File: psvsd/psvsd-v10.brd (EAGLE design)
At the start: 30 x 33.4 mm, 30 parts, among them J1 TRANSFLASH-PUSH, U1 USB2244QFN, U3 VREG, Y1 24.000MHz

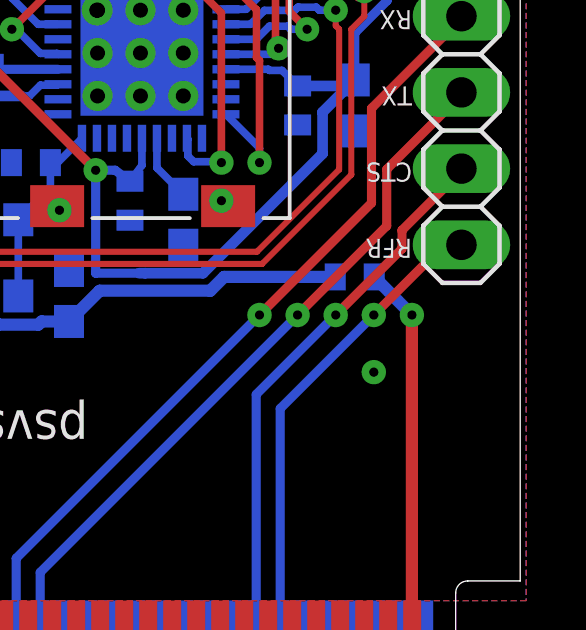
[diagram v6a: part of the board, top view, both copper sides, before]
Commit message: Extended ground plane on top layer to even electric properties
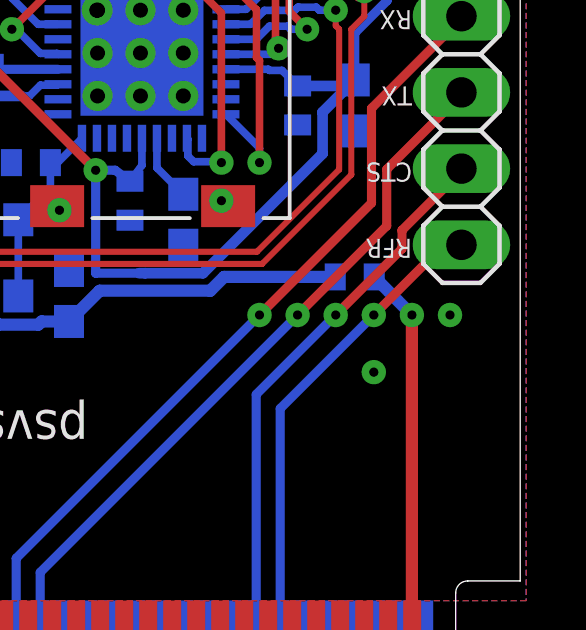
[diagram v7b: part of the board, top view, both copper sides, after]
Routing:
- net GND: vias 20 -> 21
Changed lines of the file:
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@@
 <via x="16.1925" y="17.4625" extent="1-16" drill="0.3048"/>
 <contactref element="R6" pad="2"/>
+<via x="29.21" y="13.97" extent="1-16" drill="0.3048"/>
+<wire x1="23.414" y1="30.75" x2="28.65" y2="32.405" width="0" layer="19" extent="1-1"/>
+<wire x1="23.1775" y1="31.33" x2="23.414" y2="30.75" width="0" layer="19" extent="1-16"/>
+<wire x1="20.97" y1="31.75" x2="23.1775" y2="31.33" width="0" layer="19" extent="16-16"/>
+<wire x1="20.32" y1="30.06" x2="20.97" y2="31.75" width="0" layer="19" extent="16-16"/>
+<wire x1="21.59" y1="29.2608" x2="20.32" y2="30.06" width="0" layer="19" extent="16-16"/>
+<wire x1="20.424" y1="28.1" x2="21.59" y2="29.2608" width="0" layer="19" extent="1-1"/>
+<wire x1="23.71" y1="27.94" x2="21.59" y2="29.2608" width="0" layer="19" extent="16-16"/>
+<wire x1="26.685" y1="26.67" x2="23.71" y2="27.94" width="0" layer="19" extent="16-16"/>
+<wire x1="29.591" y1="26.47" x2="26.685" y2="26.67" width="0" layer="19" extent="16-16"/>
+<wire x1="17.942" y1="25.46" x2="20.424" y2="28.1" width="0" layer="19" extent="1-16"/>
 <wire x1="18.89125" y1="24.13" x2="18.415" y2="24.430025" width="0" layer="19" extent="16-16"/>
-<wire x1="21.59" y1="17.78" x2="21.814" y2="17.6" width="0" layer="19" extent="1-1"/>
-<wire x1="16.35" y1="3.255" x2="15.95" y2="3.255" width="0" layer="19" extent="1-16"/>
-<wire x1="23.1775" y1="31.33" x2="23.414" y2="30.75" width="0" layer="19" extent="1-16"/>
-<wire x1="17.1125125" y1="24.7325125" x2="17.4371" y2="24.13" width="0" layer="19" extent="16-16"/>
+<wire x1="17.1125125" y1="24.7325125" x2="17.9718" y2="24.873225" width="0" layer="19" extent="16-16"/>
+<wire x1="17.4371" y1="24.13" x2="17.1125125" y2="24.7325125" width="0" layer="19" extent="16-16"/>
+<wire x1="17.4625" y1="24.13" x2="17.4371" y2="24.13" width="0" layer="19" extent="1-1"/>
+<wire x1="18.89125" y1="22.70125" x2="18.415" y2="23.495" width="0" layer="19" extent="16-16"/>
+<wire x1="18.942" y1="22.66" x2="18.89125" y2="22.70125" width="0" layer="19" extent="16-16"/>
+<wire x1="17.4625" y1="22.70125" x2="18.415" y2="23.495" width="0" layer="19" extent="16-16"/>
+<wire x1="20.32" y1="22.70125" x2="18.942" y2="22.66" width="0" layer="19" extent="16-16"/>
+<wire x1="18.89125" y1="21.2725" x2="18.942" y2="22.66" width="0" layer="19" extent="16-16"/>
+<wire x1="20.32" y1="24.13" x2="18.89125" y2="24.13" width="0" layer="19" extent="1-1"/>
+<wire x1="20.32" y1="21.2725" x2="20.32" y2="22.70125" width="0" layer="19" extent="1-1"/>
+<wire x1="17.4625" y1="21.2725" x2="17.4625" y2="22.70125" width="0" layer="19" extent="1-1"/>
+<wire x1="14.59" y1="19.05" x2="17.4625" y2="21.2725" width="0" layer="19" extent="16-16"/>
+<wire x1="13.335" y1="19.05" x2="14.59" y2="19.05" width="0" layer="19" extent="16-16"/>
+<wire x1="12.28" y1="20.32" x2="13.335" y2="19.05" width="0" layer="19" extent="16-16"/>
+<wire x1="13.12" y1="17.145" x2="13.335" y2="19.05" width="0" layer="19" extent="16-16"/>
+<wire x1="12.685" y1="22.225" x2="12.28" y2="20.32" width="0" layer="19" extent="16-16"/>
+<wire x1="12.3825" y1="23.495" x2="12.685" y2="22.225" width="0" layer="19" extent="16-16"/>
+<wire x1="16.114" y1="17.6" x2="14.59" y2="19.05" width="0" layer="19" extent="1-16"/>
+<wire x1="16.1925" y1="17.4625" x2="16.114" y2="17.6" width="0" layer="19" extent="1-1"/>
+<wire x1="16.51" y1="15.455" x2="16.1925" y2="17.4625" width="0" layer="19" extent="16-16"/>
+<wire x1="18.542" y1="17.13" x2="16.1925" y2="17.4625" width="0" layer="19" extent="16-16"/>
+<wire x1="20.32" y1="16.295" x2="18.542" y2="17.13" width="0" layer="19" extent="16-16"/>
+<wire x1="21.59" y1="17.78" x2="20.32" y2="16.295" width="0" layer="19" extent="16-16"/>
+<wire x1="21.814" y1="17.6" x2="21.59" y2="17.78" width="0" layer="19" extent="1-1"/>
+<wire x1="10.1299" y1="25.4" x2="12.3825" y2="23.495" width="0" layer="19" extent="16-16"/>
+<wire x1="9.31" y1="28.575" x2="10.1299" y2="25.4" width="0" layer="19" extent="16-16"/>
+<wire x1="9.31" y1="31.115" x2="9.31" y2="28.575" width="0" layer="19" extent="16-16"/>
+<wire x1="10.014" y1="31.75" x2="9.31" y2="31.115" width="0" layer="19" extent="1-16"/>
+<wire x1="9.51" y1="33.02" x2="10.014" y2="31.75" width="0" layer="19" extent="1-16"/>
+<wire x1="12.3825" y1="31.115" x2="10.014" y2="31.75" width="0" layer="19" extent="1-1"/>
+<wire x1="12.7" y1="29.425" x2="12.3825" y2="31.115" width="0" layer="19" extent="16-16"/>
+<wire x1="13.716" y1="32.4" x2="12.3825" y2="31.115" width="0" layer="19" extent="16-16"/>
+<wire x1="6.35" y1="27.94" x2="9.31" y2="28.575" width="0" layer="19" extent="16-16"/>
+<wire x1="3.516" y1="26.53" x2="6.35" y2="27.94" width="0" layer="19" extent="1-1"/>
+<wire x1="24.13" y1="20.305" x2="21.59" y2="17.78" width="0" layer="19" extent="16-16"/>
+<wire x1="26.035" y1="20.105" x2="24.13" y2="20.305" width="0" layer="19" extent="16-16"/>
+<wire x1="11.43" y1="13.335" x2="13.12" y2="17.145" width="0" layer="19" extent="16-16"/>
+<wire x1="4.45" y1="32.405" x2="6.35" y2="27.94" width="0" layer="19" extent="1-1"/>
+<wire x1="29.21" y1="13.97" x2="26.035" y2="20.105" width="0" layer="19" extent="16-16"/>
+<wire x1="26.67" y1="12.065" x2="29.21" y2="13.97" width="0" layer="19" extent="1-1"/>
+<wire x1="3.81" y1="13.335" x2="11.43" y2="13.335" width="0" layer="19" extent="1-1"/>
+<wire x1="25.15" y1="3.255" x2="26.67" y2="12.065" width="0" layer="19" extent="16-16"/>
+<wire x1="21.15" y1="3.255" x2="25.15" y2="3.255" width="0" layer="19" extent="16-16"/>
+<wire x1="19.15" y1="3.255" x2="21.15" y2="3.255" width="0" layer="19" extent="1-16"/>
+<wire x1="17.15" y1="3.255" x2="19.15" y2="3.255" width="0" layer="19" extent="1-16"/>
+<wire x1="16.35" y1="3.255" x2="17.15" y2="3.255" width="0" layer="19" extent="16-16"/>
+<wire x1="15.95" y1="3.255" x2="16.35" y2="3.255" width="0" layer="19" extent="1-16"/>
+<wire x1="9.55" y1="3.255" x2="15.95" y2="3.255" width="0" layer="19" extent="1-1"/>
+<wire x1="7.3198" y1="3.4248" x2="9.55" y2="3.255" width="0" layer="19" extent="1-1"/>
+<wire x1="6.75" y1="3.255" x2="7.15" y2="3.255" width="0" layer="19" extent="1-16"/>
+<wire x1="5.95" y1="3.255" x2="6.75" y2="3.255" width="0" layer="19" extent="16-16"/>
+<wire x1="5.15" y1="3.255" x2="5.95" y2="3.255" width="0" layer="19" extent="16-16"/>
+<wire x1="4.75" y1="3.255" x2="5.15" y2="3.255" width="0" layer="19" extent="1-16"/>
 </signal>
 <signal name="+5V">

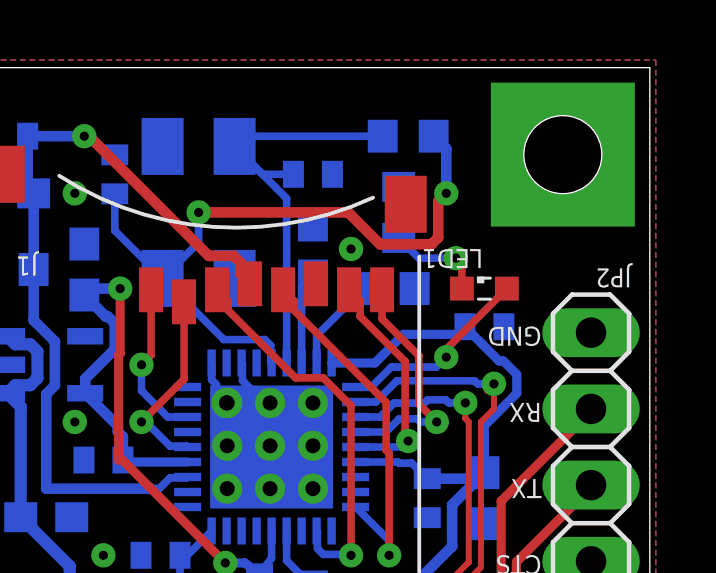
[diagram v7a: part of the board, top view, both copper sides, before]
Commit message: Added value for LED
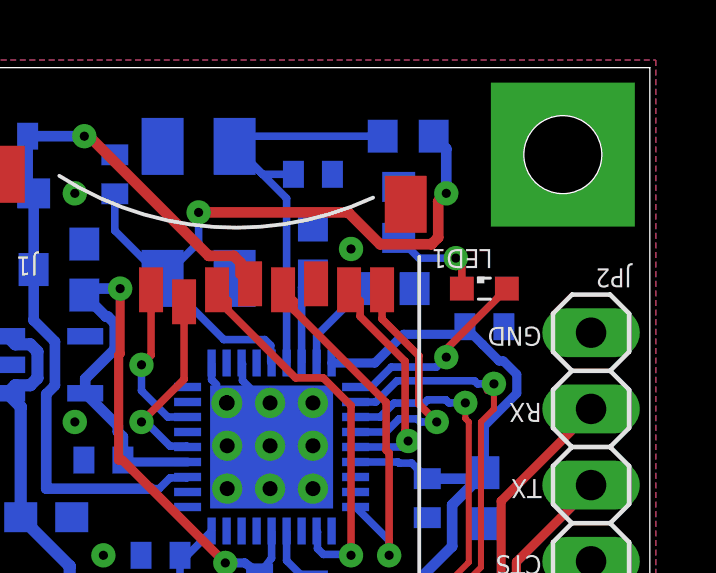
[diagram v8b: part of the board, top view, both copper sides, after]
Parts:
- LED1: value (none) -> BLUE
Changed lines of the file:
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@@
 <layer number="35" name="tGlue" color="7" fill="4" visible="no" active="yes"/>
 <layer number="36" name="bGlue" color="7" fill="5" visible="no" active="yes"/>
-<layer number="37" name="tTest" color="7" fill="1" visible="yes" active="yes"/>
-<layer number="38" name="bTest" color="7" fill="1" visible="yes" active="yes"/>
+<layer number="37" name="tTest" color="7" fill="1" visible="no" active="yes"/>
+<layer number="38" name="bTest" color="7" fill="1" visible="no" active="yes"/>
 <layer number="39" name="tKeepout" color="4" fill="11" visible="yes" active="yes"/>
 <layer number="40" name="bKeepout" color="1" fill="11" visible="yes" active="yes"/>
@@
 <layer number="42" name="bRestrict" color="1" fill="10" visible="yes" active="yes"/>
 <layer number="43" name="vRestrict" color="2" fill="10" visible="yes" active="yes"/>
-<layer number="44" name="Drills" color="7" fill="1" visible="yes" active="yes"/>
-<layer number="45" name="Holes" color="7" fill="1" visible="yes" active="yes"/>
-<layer number="46" name="Milling" color="3" fill="1" visible="yes" active="yes"/>
-<layer number="47" name="Measures" color="7" fill="1" visible="yes" active="yes"/>
-<layer number="48" name="Document" color="7" fill="1" visible="yes" active="yes"/>
-<layer number="49" name="Reference" color="7" fill="1" visible="yes" active="yes"/>
+<layer number="44" name="Drills" color="7" fill="1" visible="no" active="yes"/>
+<layer number="45" name="Holes" color="7" fill="1" visible="no" active="yes"/>
+<layer number="46" name="Milling" color="3" fill="1" visible="no" active="yes"/>
+<layer number="47" name="Measures" color="7" fill="1" visible="no" active="yes"/>
+<layer number="48" name="Document" color="7" fill="1" visible="no" active="yes"/>
+<layer number="49" name="Reference" color="7" fill="1" visible="no" active="yes"/>
 <layer number="50" name="dxf" color="7" fill="1" visible="no" active="no"/>
 <layer number="51" name="tDocu" color="7" fill="1" visible="yes" active="yes"/>
@@
 <attribute name="VALUE" x="11.43" y="33.3375" size="0.508" layer="28" rot="SMR180"/>
 </element>
-<element name="LED1" library="led" package="SML0603" value="" x="26.035" y="27.94" smashed="yes">
-<attribute name="NAME" x="25.9875" y="29.2575" size="0.635" layer="25" rot="SR180"/>
-<attribute name="VALUE" x="25.035" y="25.94" size="1.27" layer="27"/>
+<element name="LED1" library="led" package="SML0603" value="BLUE" x="26.035" y="27.94" smashed="yes">
+<attribute name="NAME" x="26.305" y="29.2575" size="0.635" layer="25" rot="SR180"/>
+<attribute name="VALUE" x="26.305" y="27.21" size="0.508" layer="27" rot="SR180"/>
 </element>
 <element name="R6" library="rcl" package="R0603" value="1K" x="23.1775" y="30.48" smashed="yes" rot="MR90">
